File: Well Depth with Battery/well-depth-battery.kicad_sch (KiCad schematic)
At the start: 63 parts, among them J1 Conn_01x02_Female, J2 Conn_01x04_Female, J3 Conn_02x04_Odd_Even, J4 Conn_01x02_Male, J6 Conn_01x04, Q1 Q_NMOS_GSD, Q2 Q_PMOS_GSD, U1 LM358, U2 LM358, U3 TL431DBZ, U4 NCP1117-5.0_SOT223, U5 ATSAMD21E17D-M, U6 MCP1793T-3302H/DC, Y1 Crystal_Small

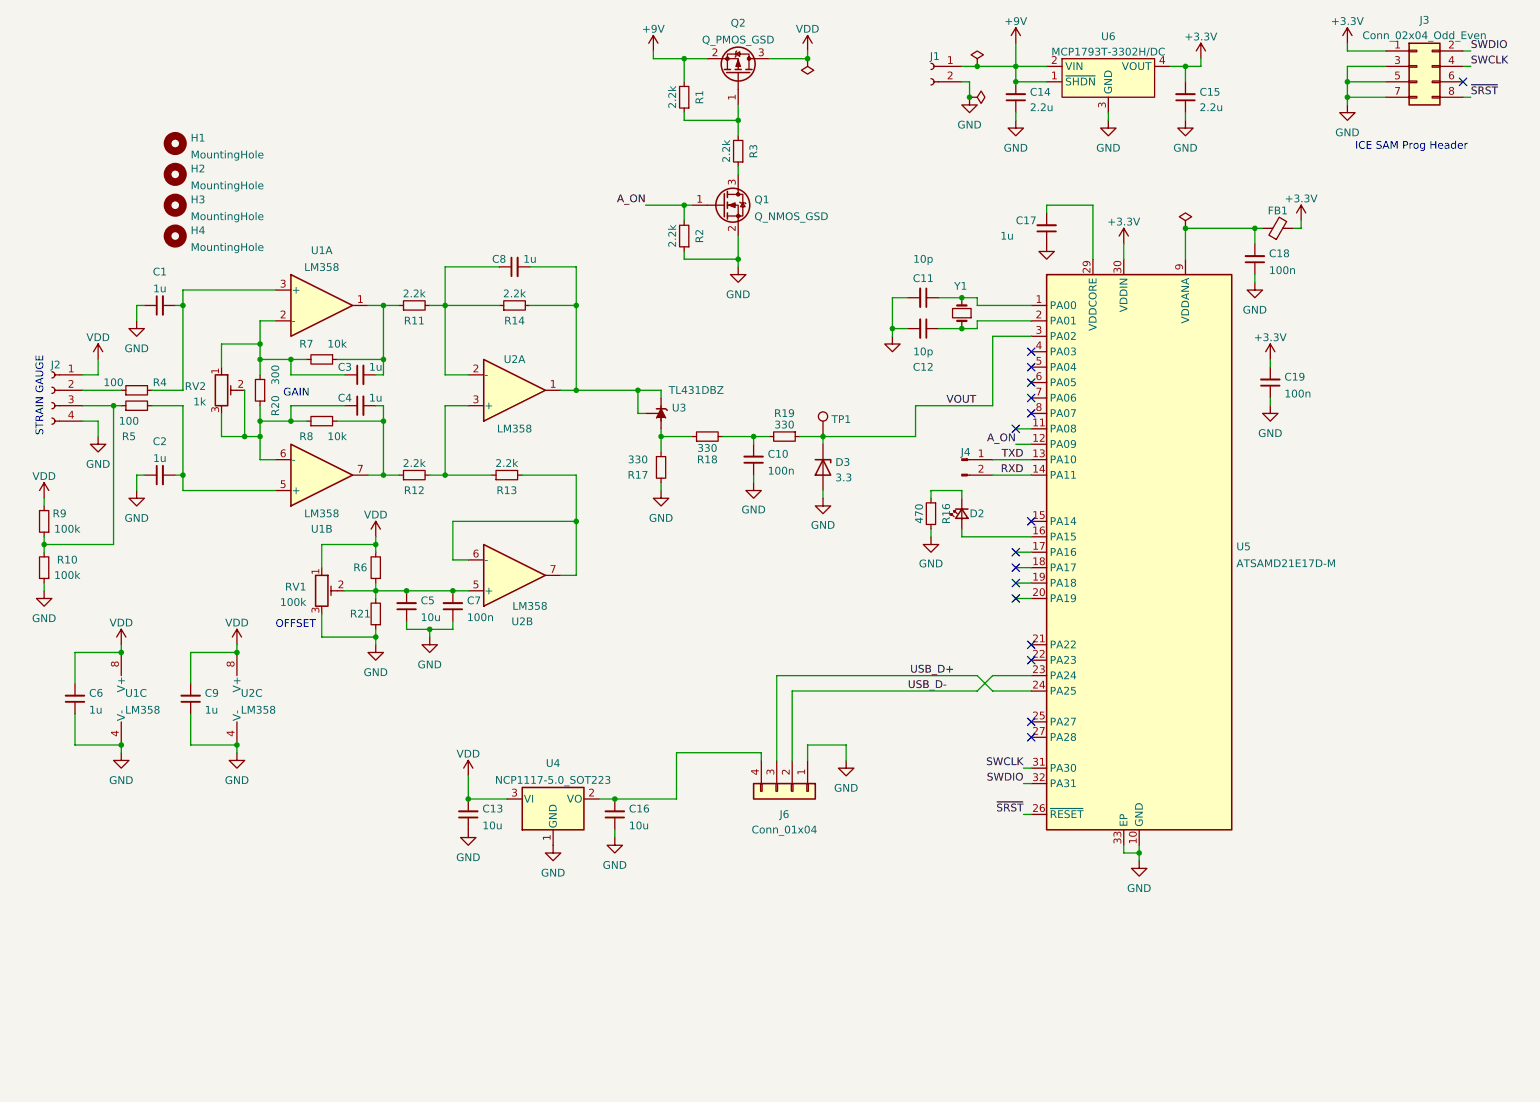
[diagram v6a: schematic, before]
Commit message: redo routing, DRC/ERC pass
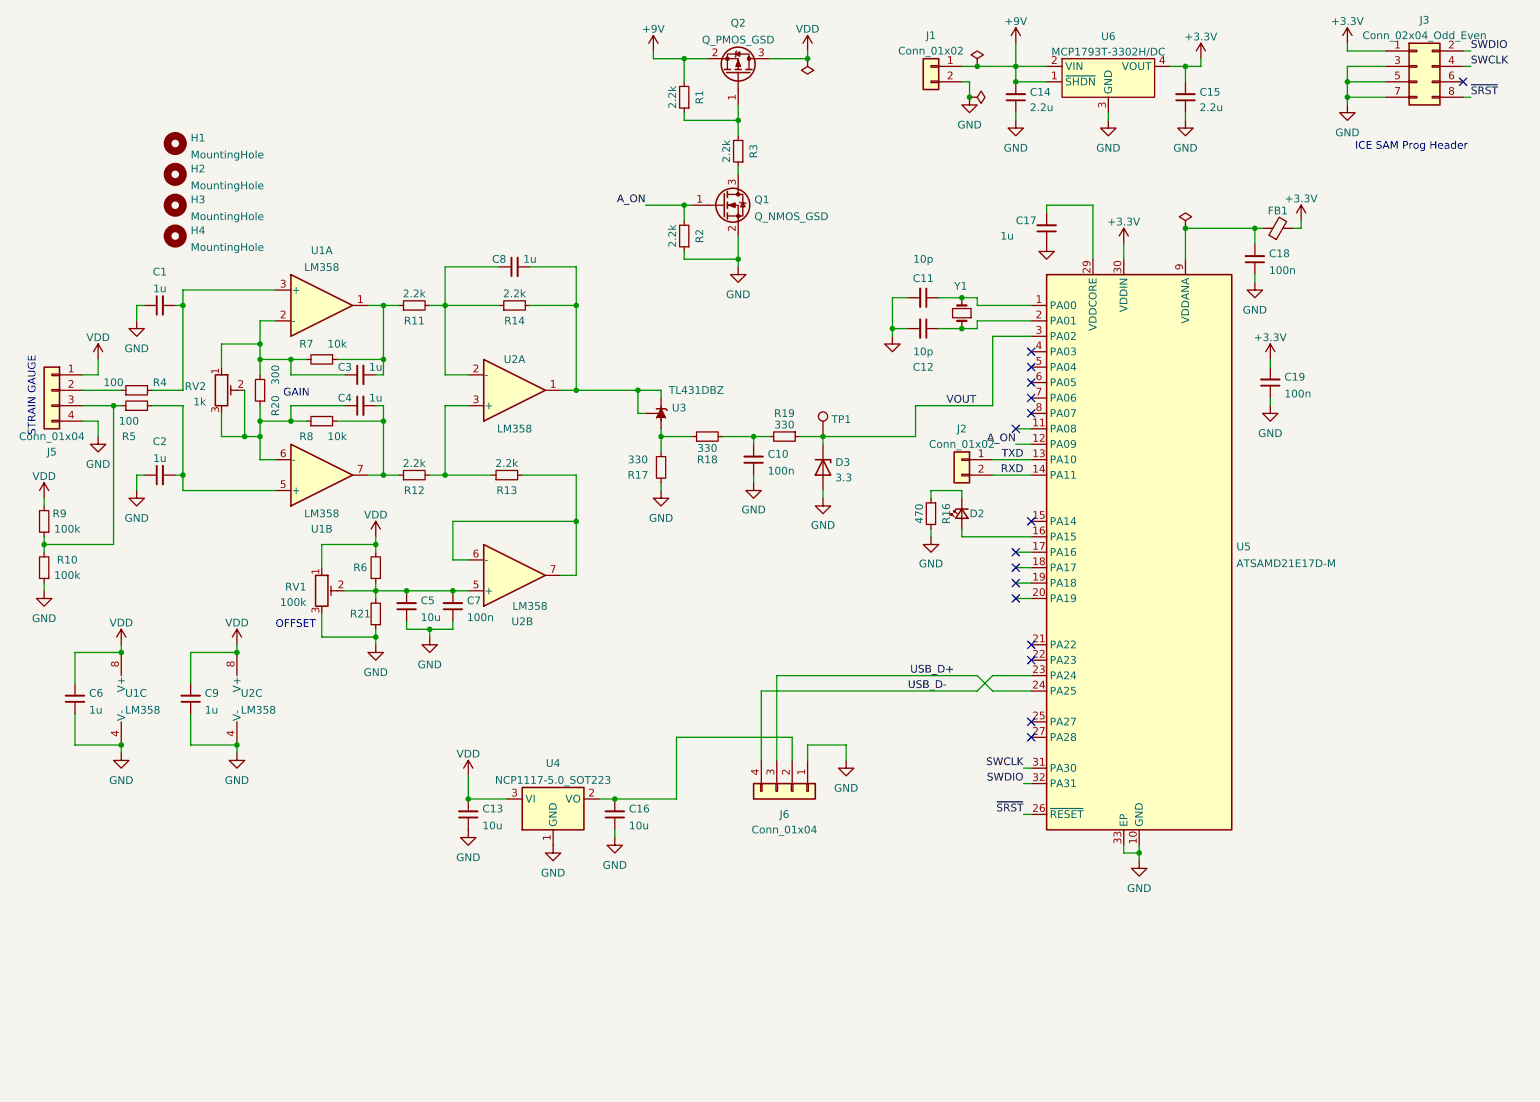
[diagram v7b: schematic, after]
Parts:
- removed J1: Conn_01x02_Female, Connector_PinHeader_2.54mm:PinHeader_1x02_P2.54mm_Vertical, symbol Connector:Conn_01x02_Female
- removed J2: Conn_01x04_Female, Connector_PinHeader_2.54mm:PinHeader_1x04_P2.54mm_Vertical, symbol Connector:Conn_01x04_Female
- removed J4: Conn_01x02_Male, Connector_PinHeader_2.54mm:PinHeader_1x02_P2.54mm_Vertical, symbol Connector:Conn_01x02_Male
- added J1, J2: Conn_01x02, Connector_PinHeader_2.54mm:PinHeader_1x02_P2.54mm_Vertical, symbol Connector_Generic:Conn_01x02
- added J5: Conn_01x04, Connector_PinHeader_2.54mm:PinHeader_1x04_P2.54mm_Vertical, symbol Connector_Generic:Conn_01x04
- C1, C10, C11, C12, C14, C15, C17, C18, C19, C2, C3, C4, C5, C6, C7, C8, C9: footprint Capacitor_SMD:C_0402_1005Metric -> Capacitor_SMD:C_0603_1608Metric
- FB1: footprint Resistor_SMD:R_0402_1005Metric -> Resistor_SMD:R_0603_1608Metric
- R1, R10, R11, R12, R13, R14, R16, R17, R18, R19, R2, R20, R21, R3, R4, R5, R6, R7, R8, R9: footprint Resistor_SMD:R_0402_1005Metric -> Capacitor_SMD:C_0603_1608Metric
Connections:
- net +9V: now also J1.1 (Pin_1)
- net GND: now also J1.2 (Pin_2), J5.4 (Pin_4)
- net RXD: now also J2.2 (Pin_2)
- net TXD: now also J2.1 (Pin_1)
- net USB_D-: now also J6.4 (Pin_4); no longer J6.2 (Pin_2)
- net VDD: now also J5.1 (Pin_1)
- net at R10.2, R5.1, R9.1: now also J5.3 (Pin_3)
- net at C16.2, U4.2 (VO): now also J6.2 (Pin_2); no longer J6.4 (Pin_4)
- net at R4.1: now also J5.2 (Pin_2)
- net +3V3 renamed +3.3V

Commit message: Fix prog connector
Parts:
- J3: footprint EWB:CardEdge_Prog -> MyParts:CardEdge_Prog
